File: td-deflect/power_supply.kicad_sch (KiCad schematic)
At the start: 77 parts, among them J13 Conn_01x02_Male, J14 Conn_01x02_Male, J18 Conn_01x02_Male, J2 Conn_01x02_Male, J3 Conn_01x04_Male, J9 Conn_01x02_Male, Q13 BSZ42DN25NS3GATMA1, Q19 BSZ42DN25NS3GATMA1, U14 LT3758AEMSE, U22 LT3758AEMSE, U32 BD9G341AEFJ, U33 BD9G341AEFJ

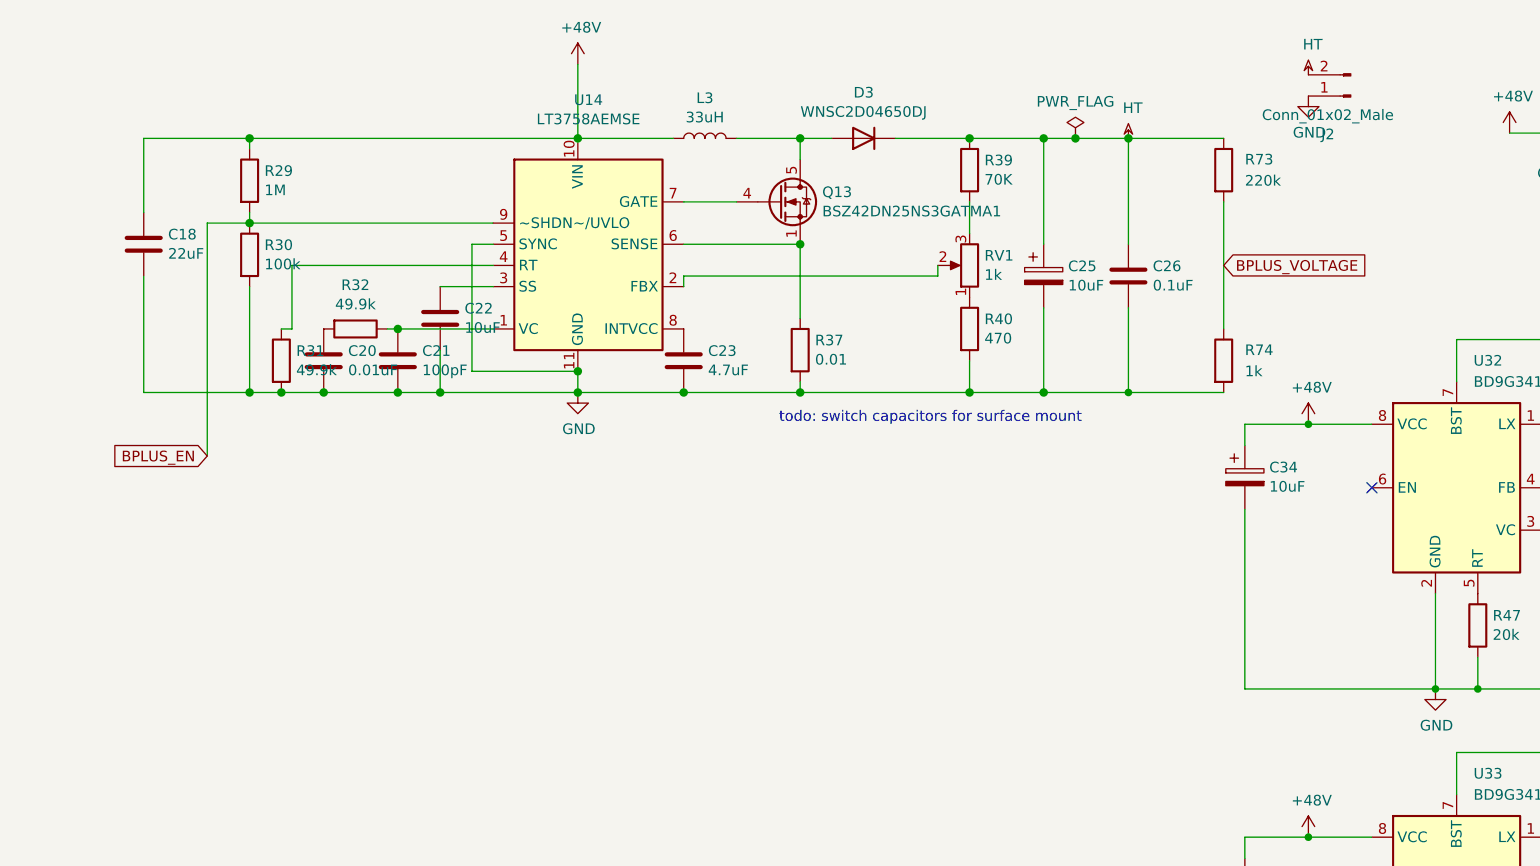
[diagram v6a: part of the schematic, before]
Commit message: use off board bplus h supply
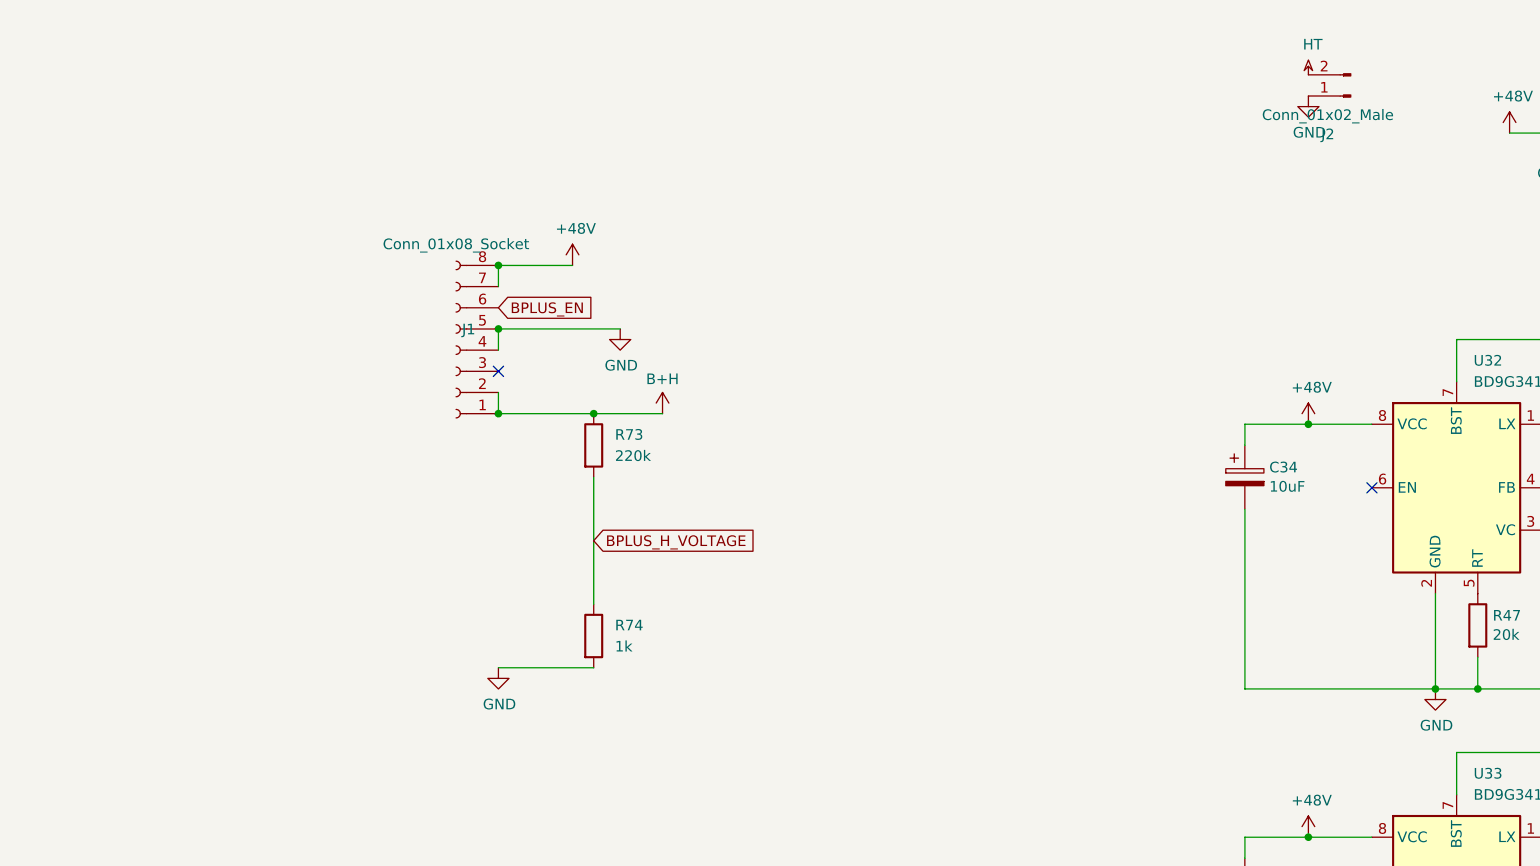
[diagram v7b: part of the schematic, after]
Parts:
- removed C18: 22uF, Capacitor_THT:CP_Radial_D8.0mm_P3.50mm, symbol Device:C
- removed C20: 0.01uF, Capacitor_SMD:C_0805_2012Metric_Pad1.18x1.45mm_HandSolder, symbol Device:C
- removed C21: 100pF, Capacitor_SMD:C_0805_2012Metric_Pad1.18x1.45mm_HandSolder, symbol Device:C
- removed C22: 10uF, Capacitor_SMD:C_1206_3216Metric_Pad1.33x1.80mm_HandSolder, symbol Device:C
- removed C23: 4.7uF, Capacitor_SMD:C_0805_2012Metric_Pad1.18x1.45mm_HandSolder, symbol Device:C
- removed C25: 10uF, Capacitor_THT:CP_Radial_D8.0mm_P3.50mm, symbol Device:CP
- removed C26: 0.1uF, Capacitor_SMD:C_1206_3216Metric_Pad1.33x1.80mm_HandSolder, symbol Device:C
- removed D3: WNSC2D04650DJ, Package_TO_SOT_SMD:TO-252-2_TabPin1, symbol Diode:1N5402
- removed L3: 33uH, Inductor_SMD:L_Bourns_SRR1260, symbol Device:L
- removed Q13: BSZ42DN25NS3GATMA1, Package_TO_SOT_SMD:TDSON-8-1, symbol Transistor_FET:BSC082N10LSG
- removed R29: 1M, Resistor_SMD:R_0805_2012Metric_Pad1.20x1.40mm_HandSolder, symbol Device:R
- removed R30: 100k, Resistor_SMD:R_0805_2012Metric_Pad1.20x1.40mm_HandSolder, symbol Device:R
- removed R31, R32: 49.9k, Resistor_SMD:R_0805_2012Metric_Pad1.20x1.40mm_HandSolder, symbol Device:R
- removed R37: 0.01, Resistor_SMD:R_0805_2012Metric_Pad1.20x1.40mm_HandSolder, symbol Device:R
- removed R39: 70K, Resistor_SMD:R_1206_3216Metric_Pad1.30x1.75mm_HandSolder, symbol Device:R
- removed R40: 470, Resistor_SMD:R_0805_2012Metric_Pad1.20x1.40mm_HandSolder, symbol Device:R
- removed RV1: 1k, Potentiometer_THT:Potentiometer_Bourns_3386P_Vertical, symbol Device:R_POT
- removed U14: LT3758AEMSE, Package_SO:MSOP-10-1EP_3x3mm_P0.5mm_EP1.68x1.88mm, symbol Regulator_Switching:LT3757AEMSE
- added J1: Conn_01x08_Socket, Connector_PinHeader_2.54mm:PinHeader_1x08_P2.54mm_Horizontal, symbol Connector:Conn_01x08_Socket
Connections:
- net +48V: now also J1.7 (Pin_7), J1.8 (Pin_8)
- net BPLUS_EN: now also J1.6 (Pin_6)
- net GND: now also J1.4 (Pin_4), J1.5 (Pin_5)
- net HT: no longer R73.1
- net BPLUS_VOLTAGE renamed BPLUS_H_VOLTAGE
- new net +3.3V: J1.1 (Pin_1), J1.2 (Pin_2), R73.1
- no-connect marks 2 -> 3
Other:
- moved on the sheet: R73, R74

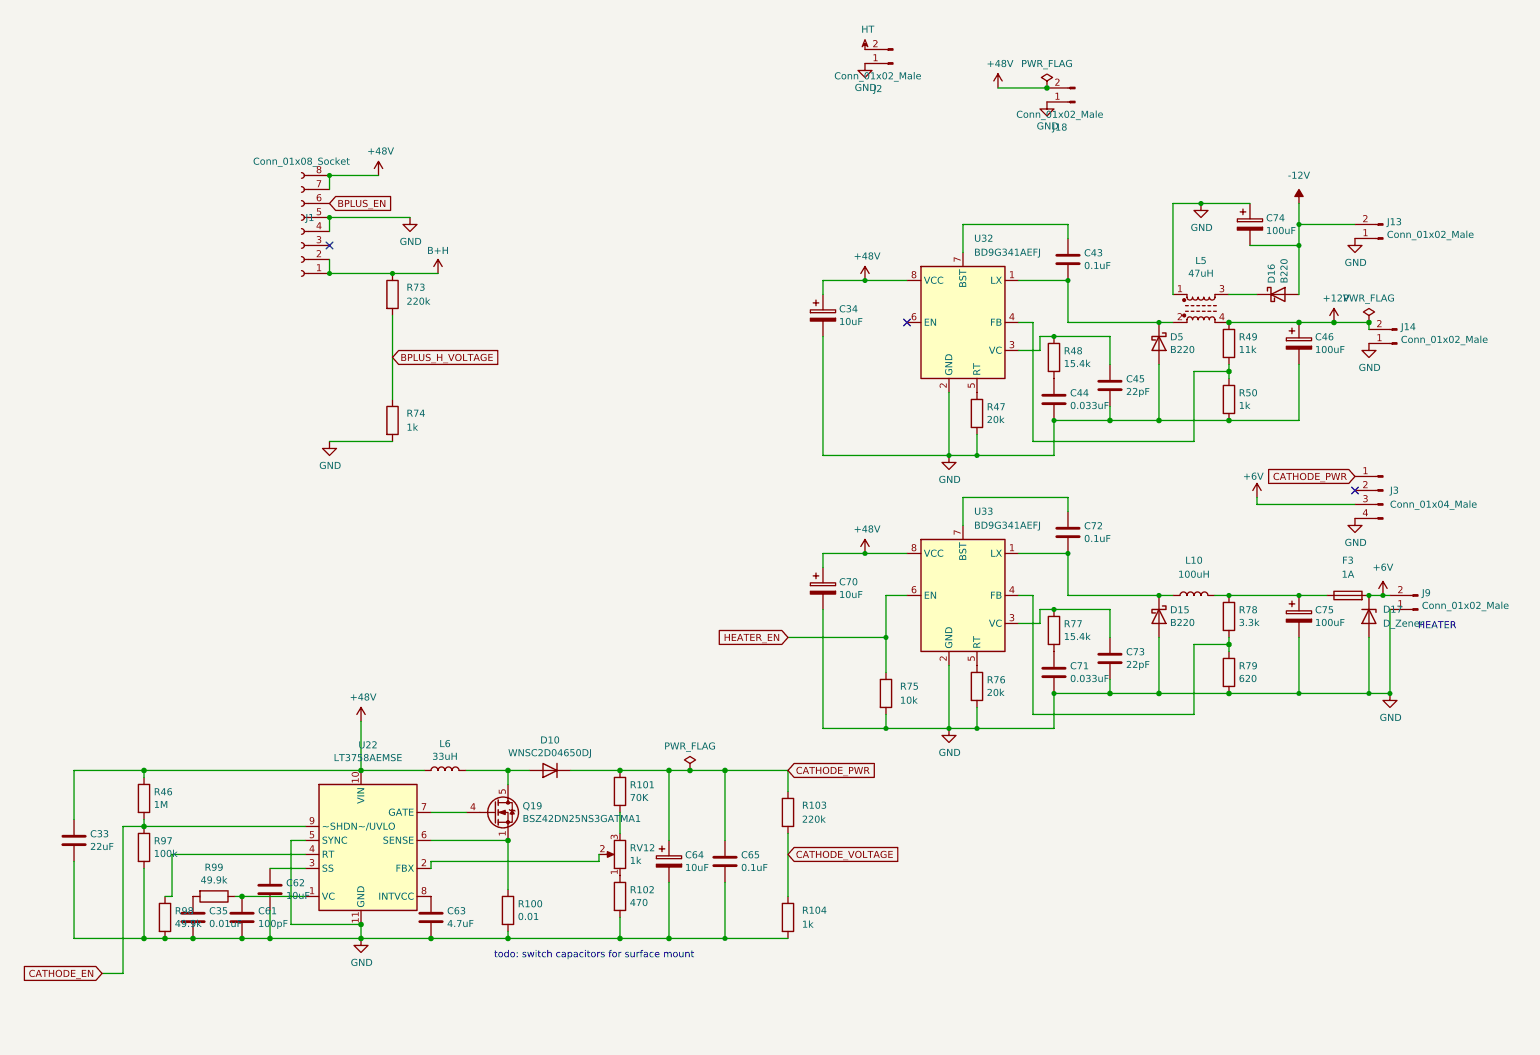
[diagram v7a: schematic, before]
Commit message: use off board f and c supply
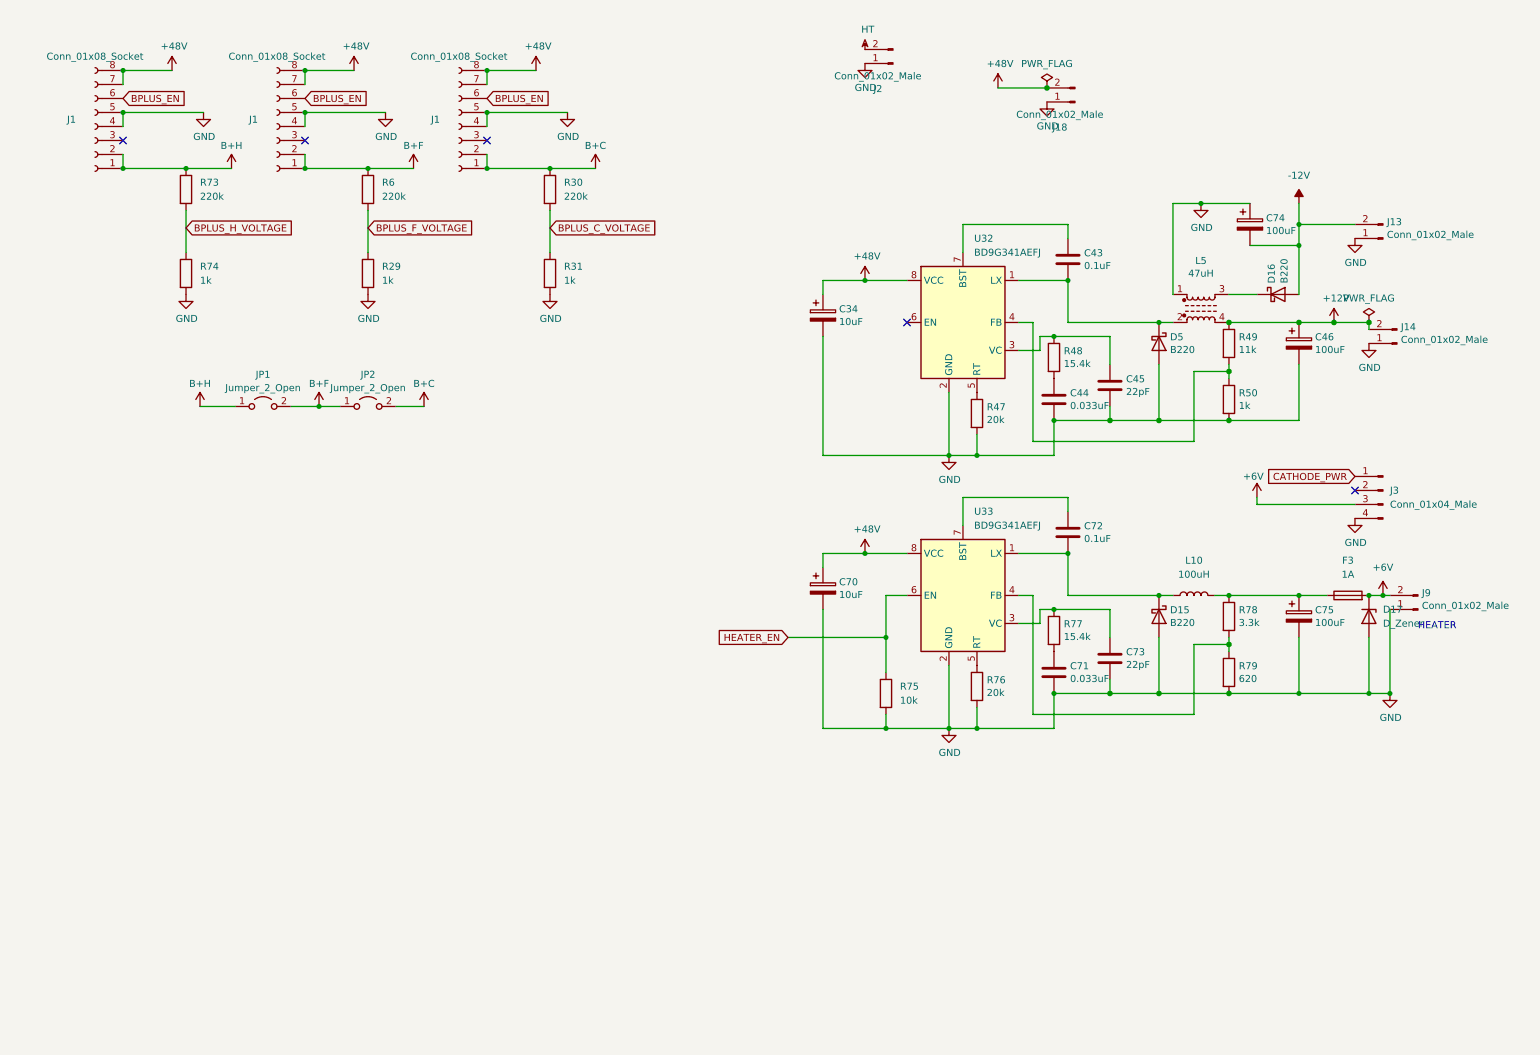
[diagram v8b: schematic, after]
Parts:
- removed C33: 22uF, Capacitor_THT:CP_Radial_D8.0mm_P3.50mm, symbol Device:C
- removed C35: 0.01uF, Capacitor_SMD:C_0805_2012Metric_Pad1.18x1.45mm_HandSolder, symbol Device:C
- removed C61: 100pF, Capacitor_SMD:C_0805_2012Metric_Pad1.18x1.45mm_HandSolder, symbol Device:C
- removed C62: 10uF, Capacitor_SMD:C_1206_3216Metric_Pad1.33x1.80mm_HandSolder, symbol Device:C
- removed C63: 4.7uF, Capacitor_SMD:C_0805_2012Metric_Pad1.18x1.45mm_HandSolder, symbol Device:C
- removed C64: 10uF, Capacitor_THT:CP_Radial_D8.0mm_P3.50mm, symbol Device:CP
- removed C65: 0.1uF, Capacitor_SMD:C_1206_3216Metric_Pad1.33x1.80mm_HandSolder, symbol Device:C
- removed D10: WNSC2D04650DJ, Package_TO_SOT_SMD:TO-252-2_TabPin1, symbol Diode:1N5402
- removed L6: 33uH, Inductor_SMD:L_Bourns_SRR1260, symbol Device:L
- removed Q19: BSZ42DN25NS3GATMA1, Package_TO_SOT_SMD:TDSON-8-1, symbol Transistor_FET:BSC082N10LSG
- removed R100: 0.01, Resistor_SMD:R_0805_2012Metric_Pad1.20x1.40mm_HandSolder, symbol Device:R
- removed R101: 70K, Resistor_SMD:R_1206_3216Metric_Pad1.30x1.75mm_HandSolder, symbol Device:R
- removed R102: 470, Resistor_SMD:R_0805_2012Metric_Pad1.20x1.40mm_HandSolder, symbol Device:R
- removed R103: 220k, Resistor_SMD:R_0805_2012Metric_Pad1.20x1.40mm_HandSolder, symbol Device:R
- removed R104: 1k, Resistor_SMD:R_0805_2012Metric_Pad1.20x1.40mm_HandSolder, symbol Device:R
- removed R46: 1M, Resistor_SMD:R_0805_2012Metric_Pad1.20x1.40mm_HandSolder, symbol Device:R
- removed R97: 100k, Resistor_SMD:R_0805_2012Metric_Pad1.20x1.40mm_HandSolder, symbol Device:R
- removed R98, R99: 49.9k, Resistor_SMD:R_0805_2012Metric_Pad1.20x1.40mm_HandSolder, symbol Device:R
- removed RV12: 1k, Potentiometer_THT:Potentiometer_Bourns_3386P_Vertical, symbol Device:R_POT
- removed U22: LT3758AEMSE, Package_SO:MSOP-10-1EP_3x3mm_P0.5mm_EP1.68x1.88mm, symbol Regulator_Switching:LT3757AEMSE
- added J1 (x2): Conn_01x08_Socket, Connector_PinHeader_2.54mm:PinHeader_1x08_P2.54mm_Horizontal, symbol Connector:Conn_01x08_Socket
- added JP1, JP2: Jumper_2_Open, symbol Jumper:Jumper_2_Open
- added R29, R31: 1k, Resistor_SMD:R_0805_2012Metric_Pad1.20x1.40mm_HandSolder, symbol Device:R
- added R30, R6: 220k, Resistor_SMD:R_0805_2012Metric_Pad1.20x1.40mm_HandSolder, symbol Device:R
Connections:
- net +3.3V: now also J1.1 (Pin_1), J1.1 (Pin_1), J1.2 (Pin_2), J1.2 (Pin_2), JP1.1 (A), JP1.2 (B), JP2.1 (A), JP2.2 (B), R30.1, R6.1
- net +48V: now also J1.7 (Pin_7), J1.7 (Pin_7), J1.8 (Pin_8), J1.8 (Pin_8)
- net BPLUS_EN: now also J1.6 (Pin_6), J1.6 (Pin_6)
- net GND: now also J1.4 (Pin_4), J1.4 (Pin_4), J1.5 (Pin_5), J1.5 (Pin_5), R29.2, R31.2
- new net BPLUS_C_VOLTAGE: R30.2, R31.1
- new net BPLUS_F_VOLTAGE: R29.1, R6.2
- no-connect marks 3 -> 5
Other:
- note removed: "todo: switch capacitors for surface mount"
- moved on the sheet: J1, R73, R74
